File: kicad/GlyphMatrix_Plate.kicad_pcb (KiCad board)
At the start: 2 copper layers, 298.3 x 128.6 mm, 6 parts

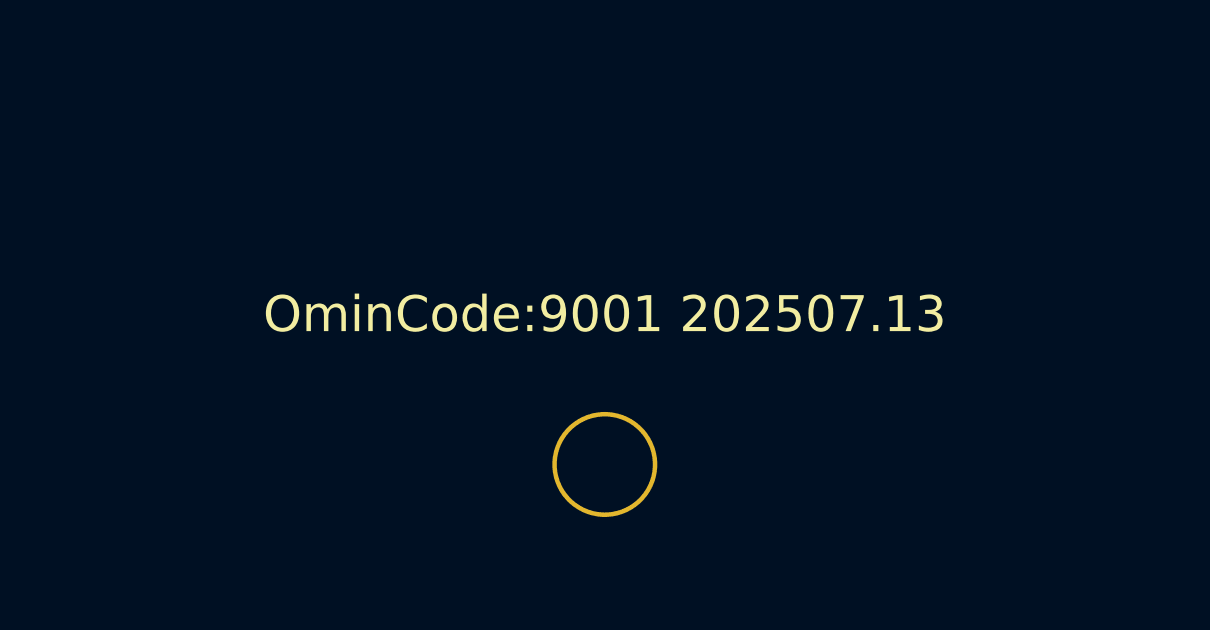
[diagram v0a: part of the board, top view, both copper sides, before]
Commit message: updated fonts (#13)
* Changed fonts for silk screen

* updated fonts for PhaseShift

* updated fonts for DeltaForm

* updated kibot for GlyphMatrix

* added dummy schematic files for GlyphMatrix

* updated kibot config

* added PhaseShift to workflow

* added DeltaForm to workflow
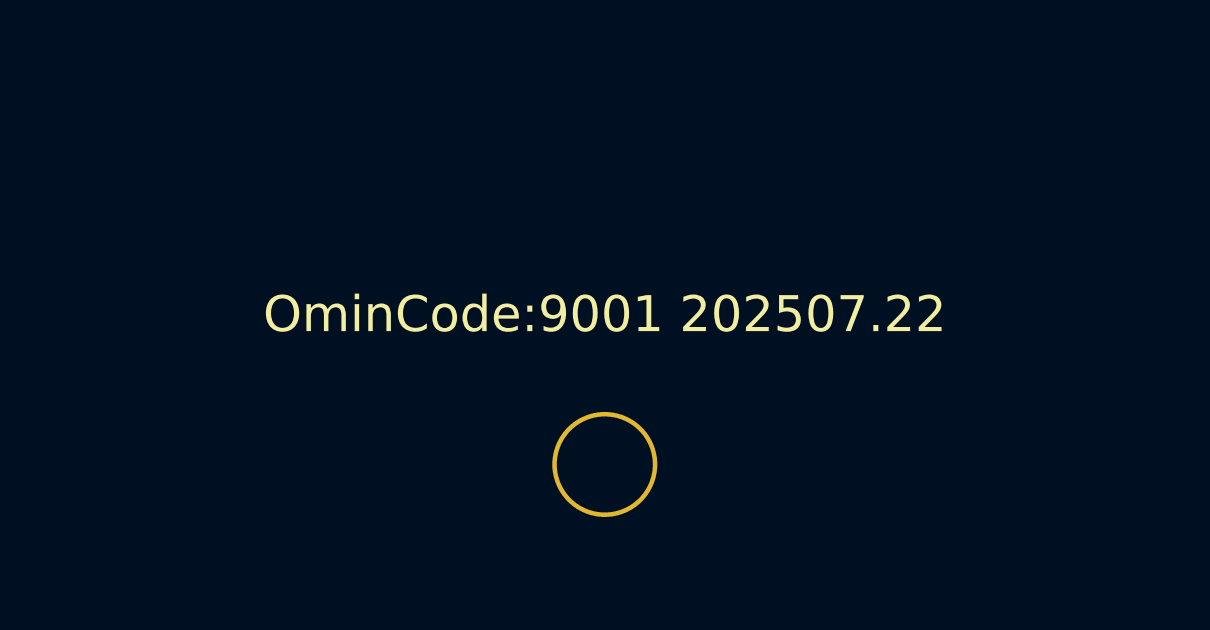
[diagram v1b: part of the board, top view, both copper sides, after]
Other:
- board text added: "OminCode:9001 202507.22"
- board text removed: "OminCode:9001 202507.13"
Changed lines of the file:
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@@
 		(layer "Edge.Cuts")
 	)
-	(gr_text "OminCode:9001 202507.13"
+	(gr_text "OminCode:9001 202507.22"
 		(at 215.23125 185.0125 0)
 		(layer "F.SilkS" knockout)

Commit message: 202508.04
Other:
- board text added: "OminCode:9001 202508.04"
- board text removed: "OminCode:9001 202507.22"
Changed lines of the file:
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@@
 		(layer "Edge.Cuts")
 	)
-	(gr_text "OminCode:9001 202507.22"
+	(gr_text "OminCode:9001 202508.04"
 		(at 215.23125 185.0125 0)
 		(layer "F.SilkS" knockout)

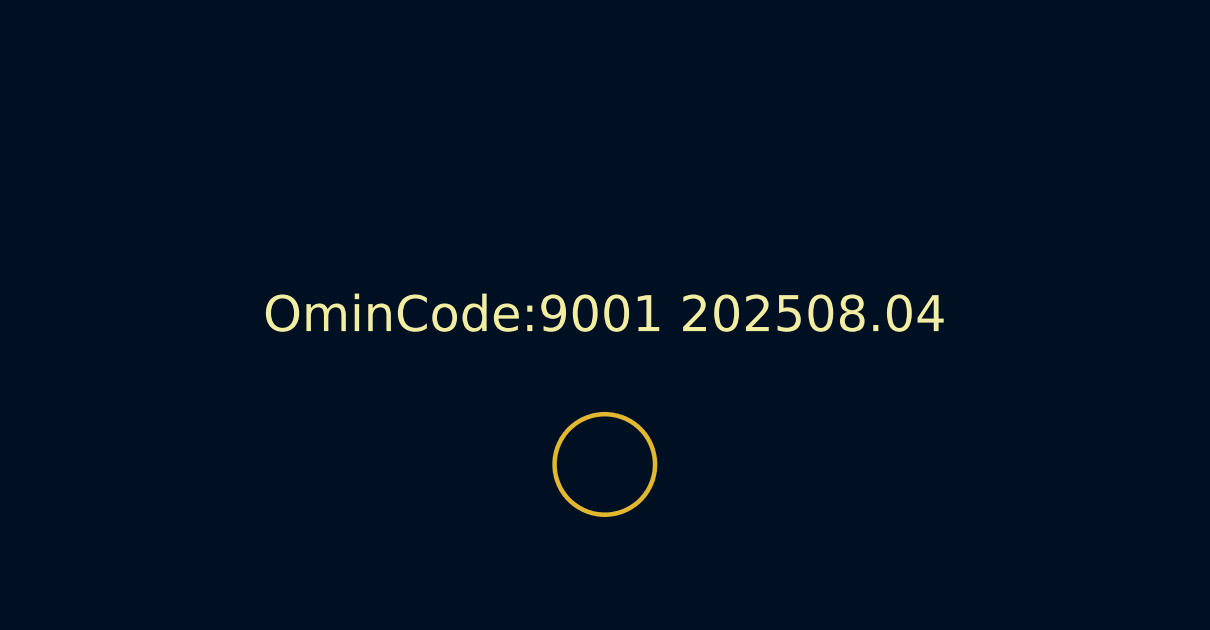
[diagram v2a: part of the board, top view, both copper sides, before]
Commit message: fixed LED for GlyphMatrix
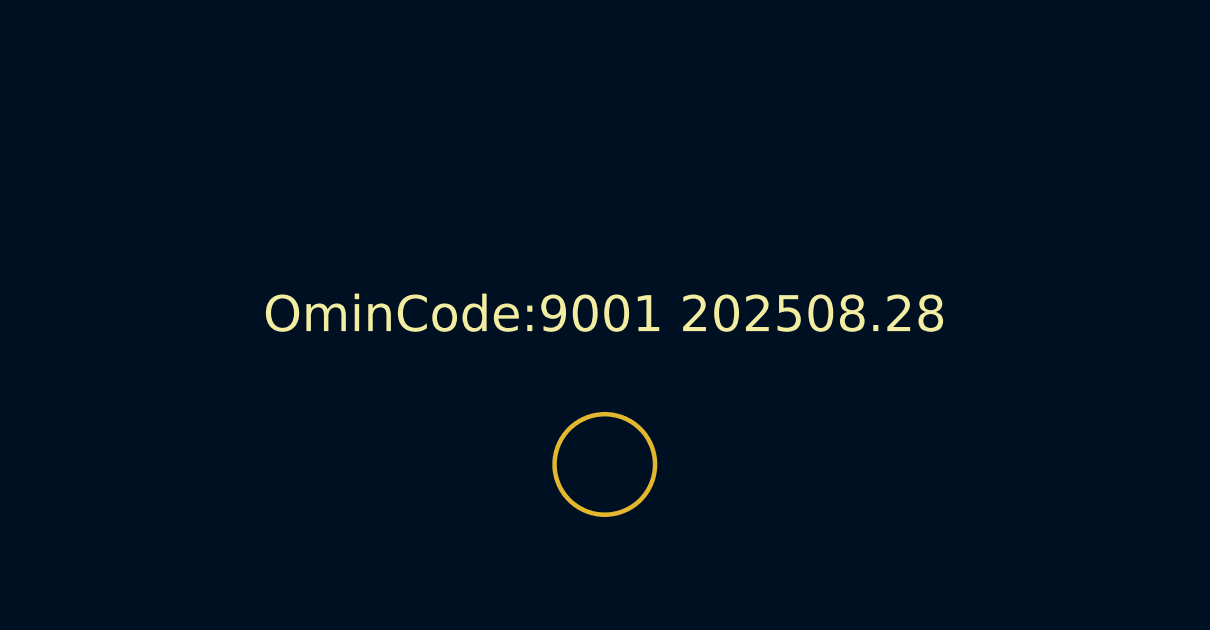
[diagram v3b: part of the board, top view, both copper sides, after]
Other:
- board text added: "BOOT"
- board text added: "OminCode:9001 202508.28"
- board text removed: "OminCode:9001 202508.04"
- board text removed: "UPDATE"
